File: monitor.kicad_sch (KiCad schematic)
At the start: 52 parts, among them J1 USB_C_Plug, J2 USB_C_Receptacle_USB2.0_14P, J3 Display, J4 Program, J5 Boot, U1 STM32U031K8Ux, U2 TPSM365R6V3RDNR, U3 TMP117xxDRV, U4 REF5025ADGK, U5 CC6903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

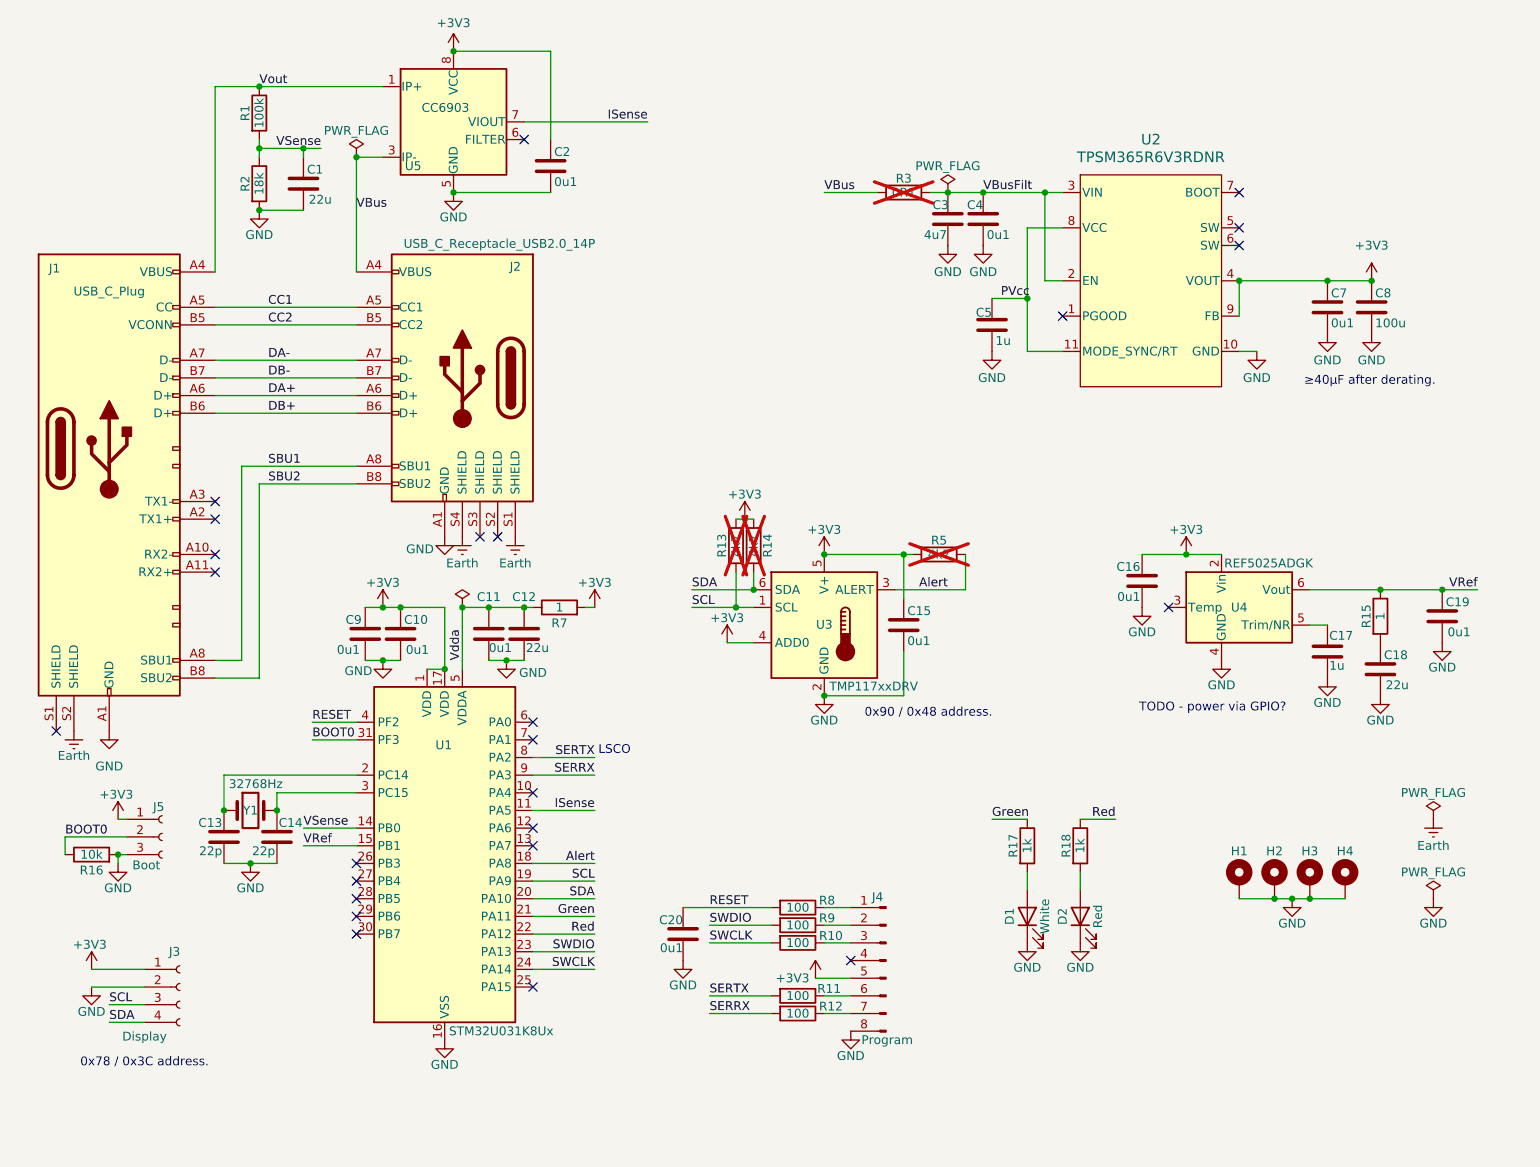
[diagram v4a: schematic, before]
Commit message: Update monitor for actual display
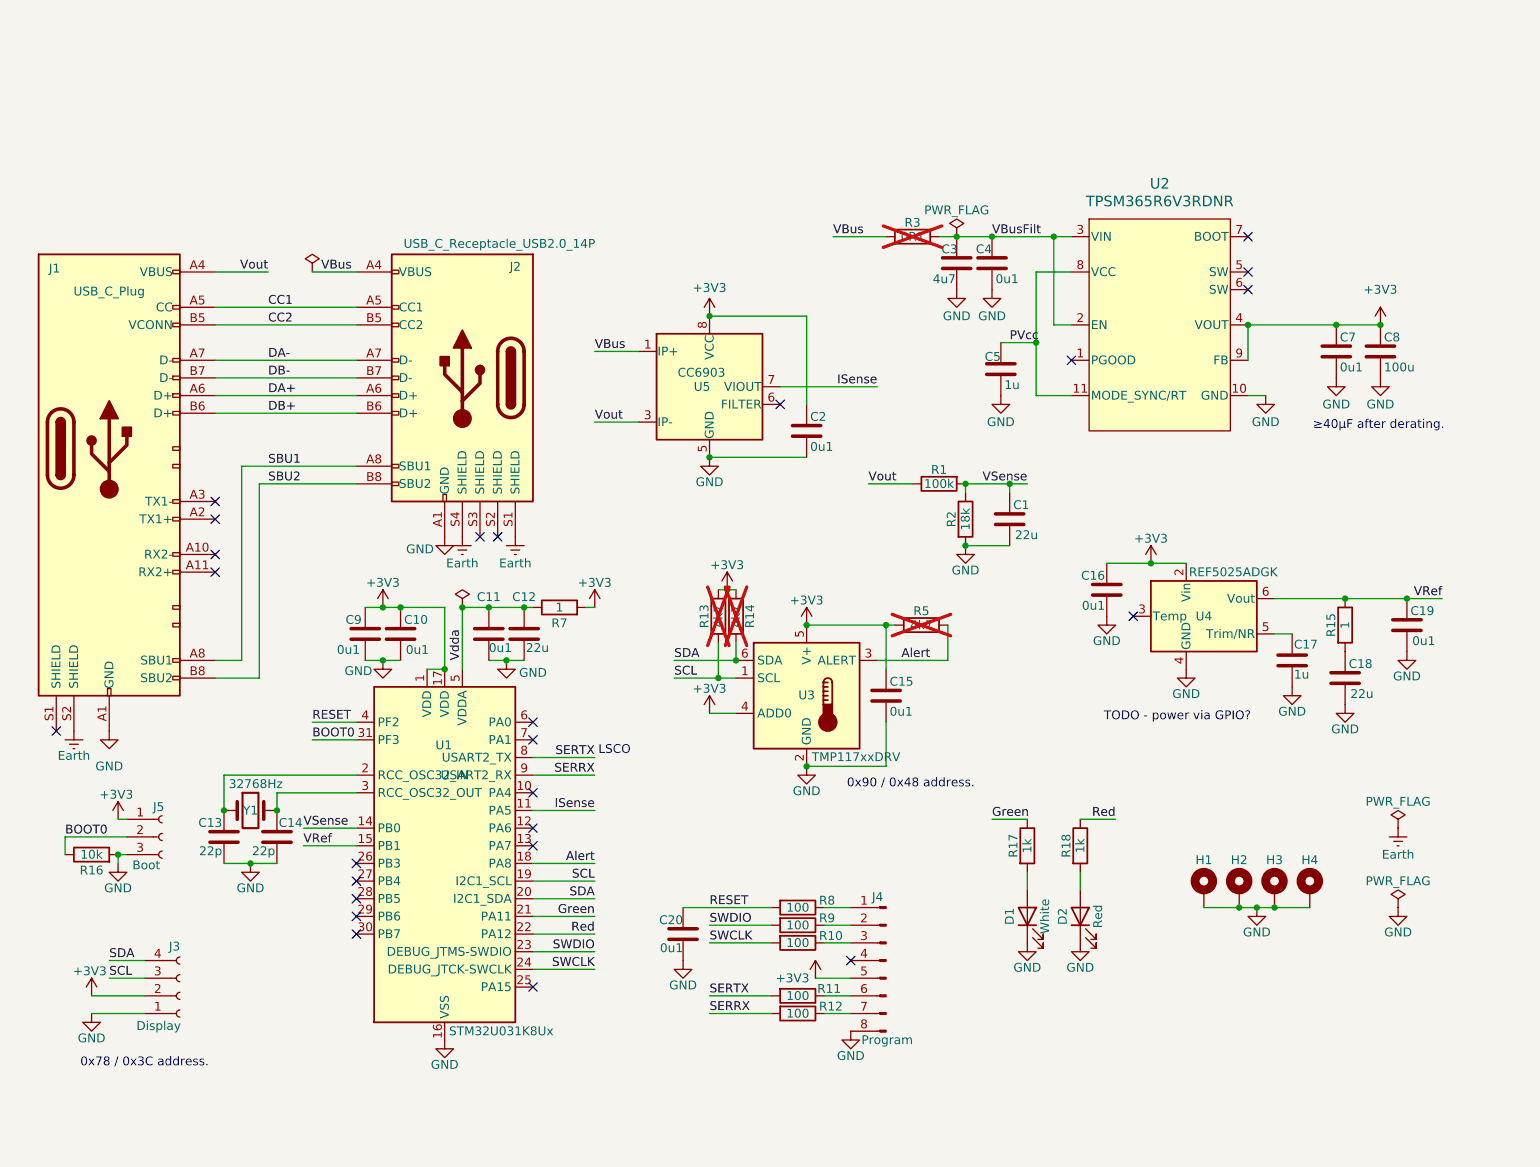
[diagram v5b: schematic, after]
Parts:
- J3: footprint Parts:PinHeader_1x04_P2.54mm_Vertical -> Connector_JST:JST_EH_B4B-EH-A_1x04_P2.50mm_Vertical
- R1: footprint Resistor_SMD:R_0603_1608Metric -> Resistor_SMD:R_0402_1005Metric; JLCPCB C25803 -> C25741
- R2: footprint Resistor_SMD:R_0603_1608Metric -> Resistor_SMD:R_0402_1005Metric; JLCPCB C25810 -> C25762
- R7: footprint Resistor_SMD:R_0402_1608Metric -> Resistor_SMD:R_0402_1005Metric
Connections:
- net +3V3: now also J3.2 (Pin_2); no longer J3.1 (Pin_1)
- net GND: now also J3.1 (Pin_1); no longer J3.2 (Pin_2)
- net VBus: now also U5.1 (IP+), U5.2 (IP+); no longer U5.3 (IP-), U5.4 (IP-)
- net Vout: now also U5.3 (IP-), U5.4 (IP-); no longer U5.1 (IP+), U5.2 (IP+)
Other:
- moved on the sheet: C1, C15, C16, C17, C18, C19, C2, C3, C4, C5, C7, C8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

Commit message: Use a 2.54mm connector footprint.
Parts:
- J3: footprint Connector_JST:JST_EH_B4B-EH-A_1x04_P2.50mm_Vertical -> Parts:PinHeader_1x04_P2.54mm_Vertical
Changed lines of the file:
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@@
 			)
 		)
-		(property "Footprint" "Connector_JST:JST_EH_B4B-EH-A_1x04_P2.50mm_Vertical"
+		(property "Footprint" "Parts:PinHeader_1x04_P2.54mm_Vertical"
 			(at 49.53 158.75 0)
 			(effects

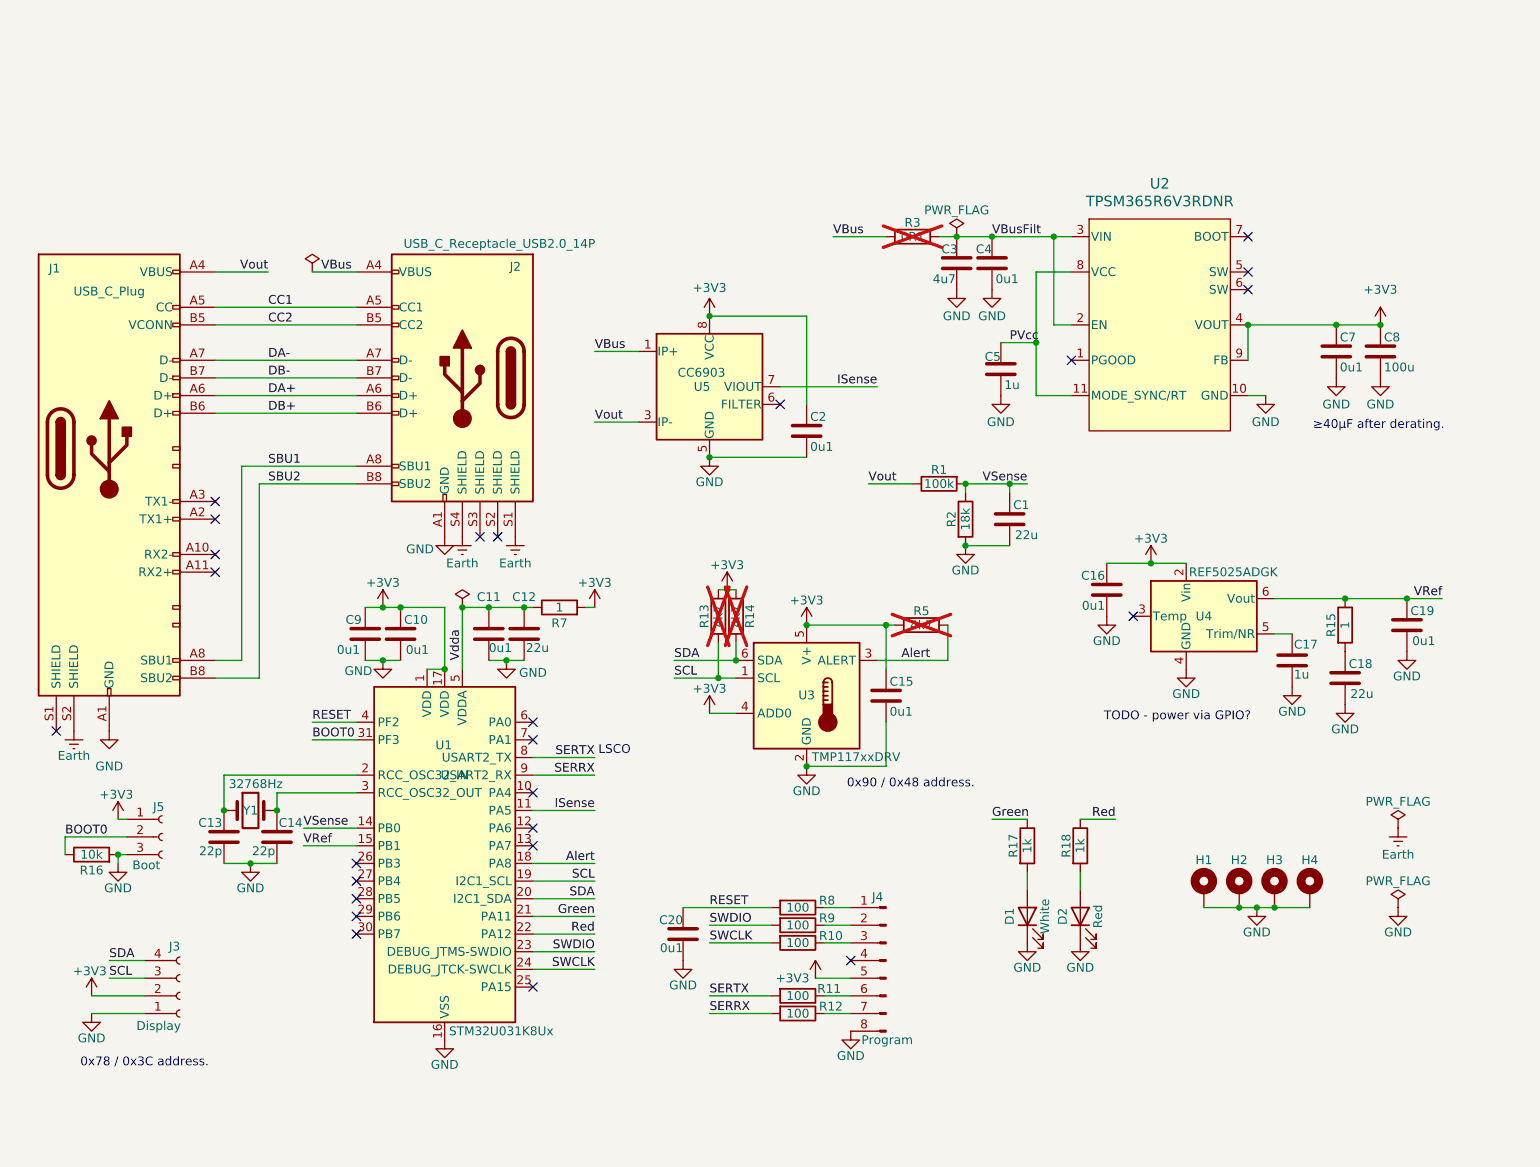
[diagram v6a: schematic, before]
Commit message: Filter ADC input.
Tweak other capacitors.
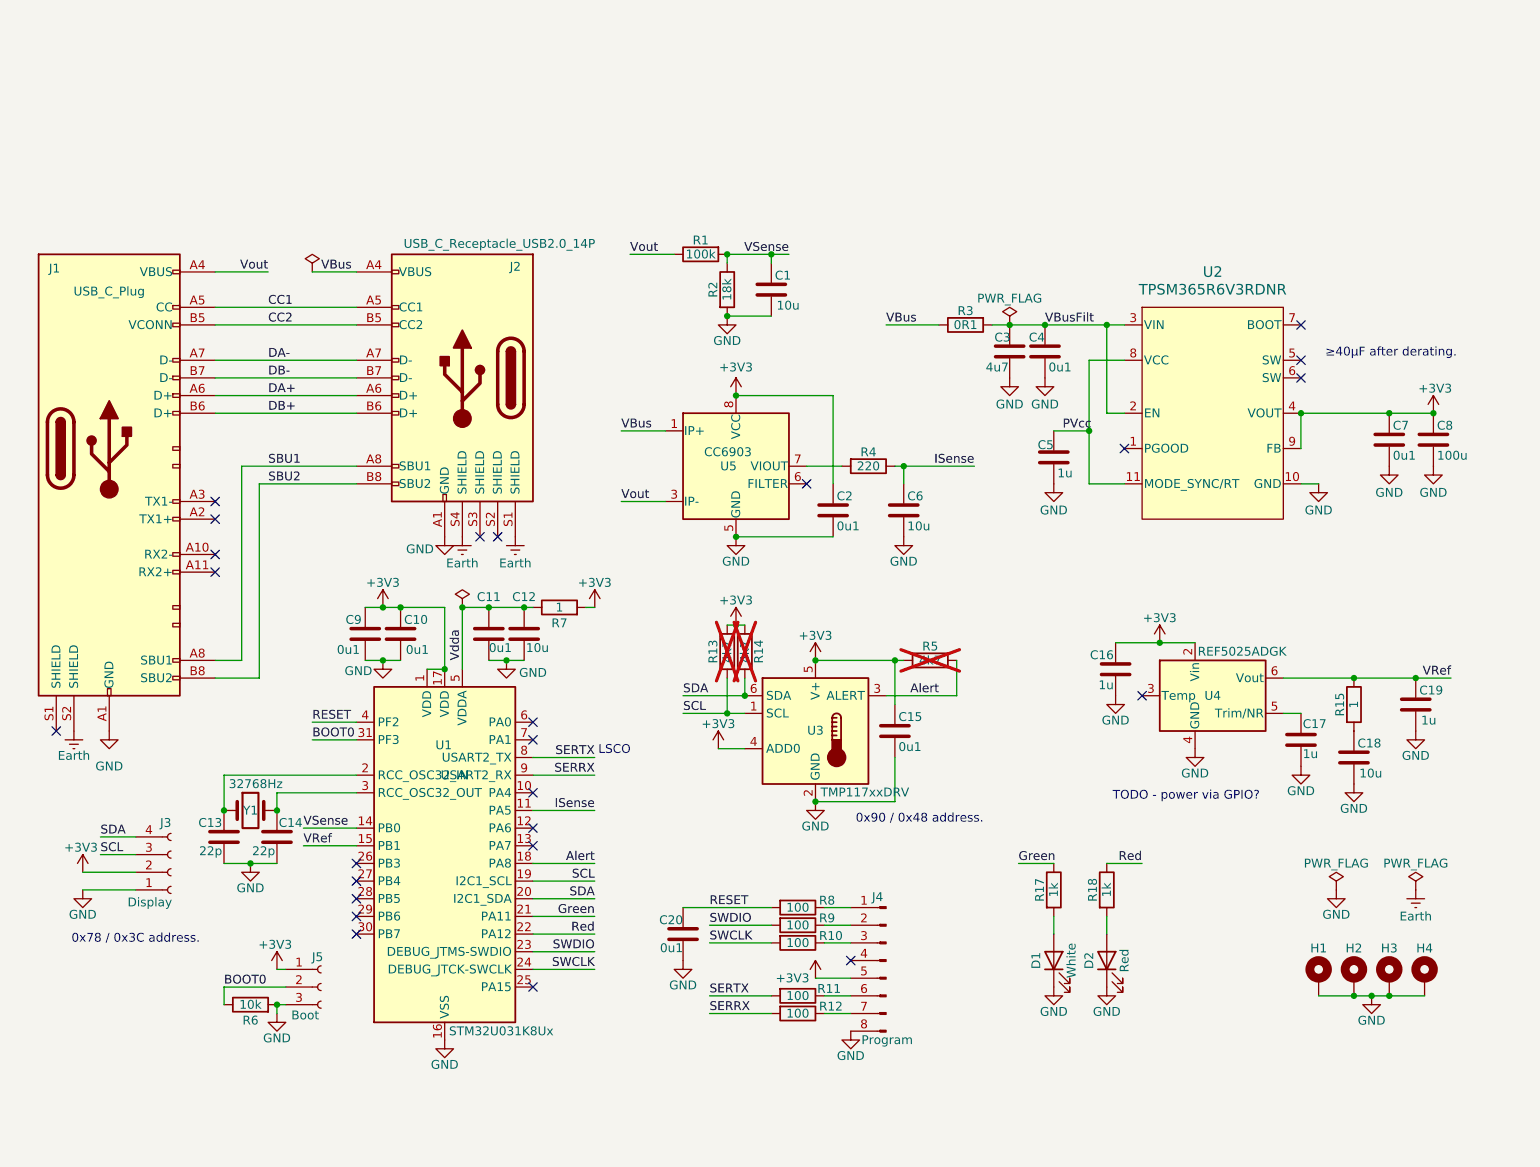
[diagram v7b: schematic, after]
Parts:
- added C6: 10u, Capacitor_SMD:C_0402_1005Metric, symbol Device:C
- added R4: 220, Resistor_SMD:R_0402_1005Metric, symbol Device:R
- C1, C12, C18: value 22u -> 10u; footprint Capacitor_SMD:C_0603_1608Metric -> Capacitor_SMD:C_0402_1005Metric; JLCPCB C59461 -> C15525
- C16, C19: value 0u1 -> 1u; JLCPCB C307331 -> C52923
- R3: now fitted
- renumbered R16 to R6
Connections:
- net GND: now also C6.2
- net ISense: now also C6.1, R4.1; no longer U5.7 (VIOUT)
- new net: R4.2, U5.7 (VIOUT)
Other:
- moved on the sheet: C1, C15, C16, C17, C18, C19, C2, C3, C4, C5, C7, C8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

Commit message: Final updates.  Ordered.
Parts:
- U1: now left out of the parts list
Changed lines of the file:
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@@
 		(unit 1)
 		(exclude_from_sim no)
-		(in_bom yes)
+		(in_bom no)
 		(on_board yes)
 		(dnp no)
